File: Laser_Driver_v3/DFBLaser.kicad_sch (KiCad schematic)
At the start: 38 parts, among them Q15 IRLML6344TRPBF, Q16 IRLML6344TRPBF, U23 OPA192IDR, U24 OPA192IDR

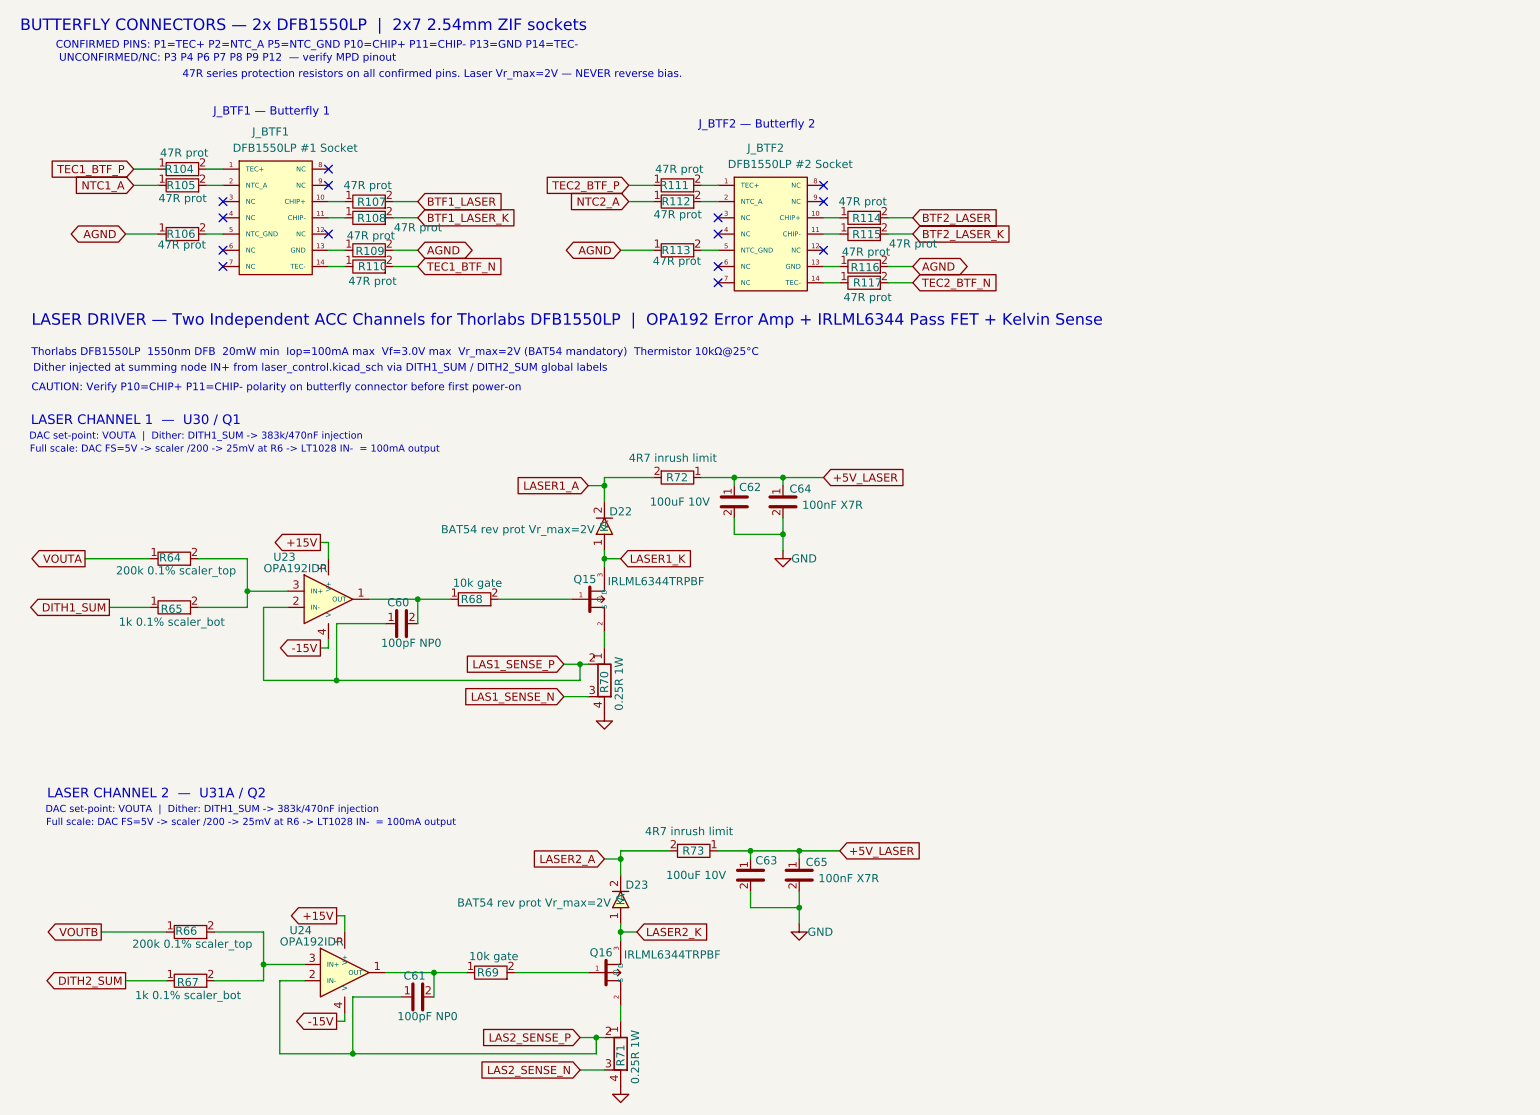
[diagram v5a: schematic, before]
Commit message: Added separate xfrmer for 6V.
Added inrush protection with NTC and increased capacitance to reduce ripple on 6V
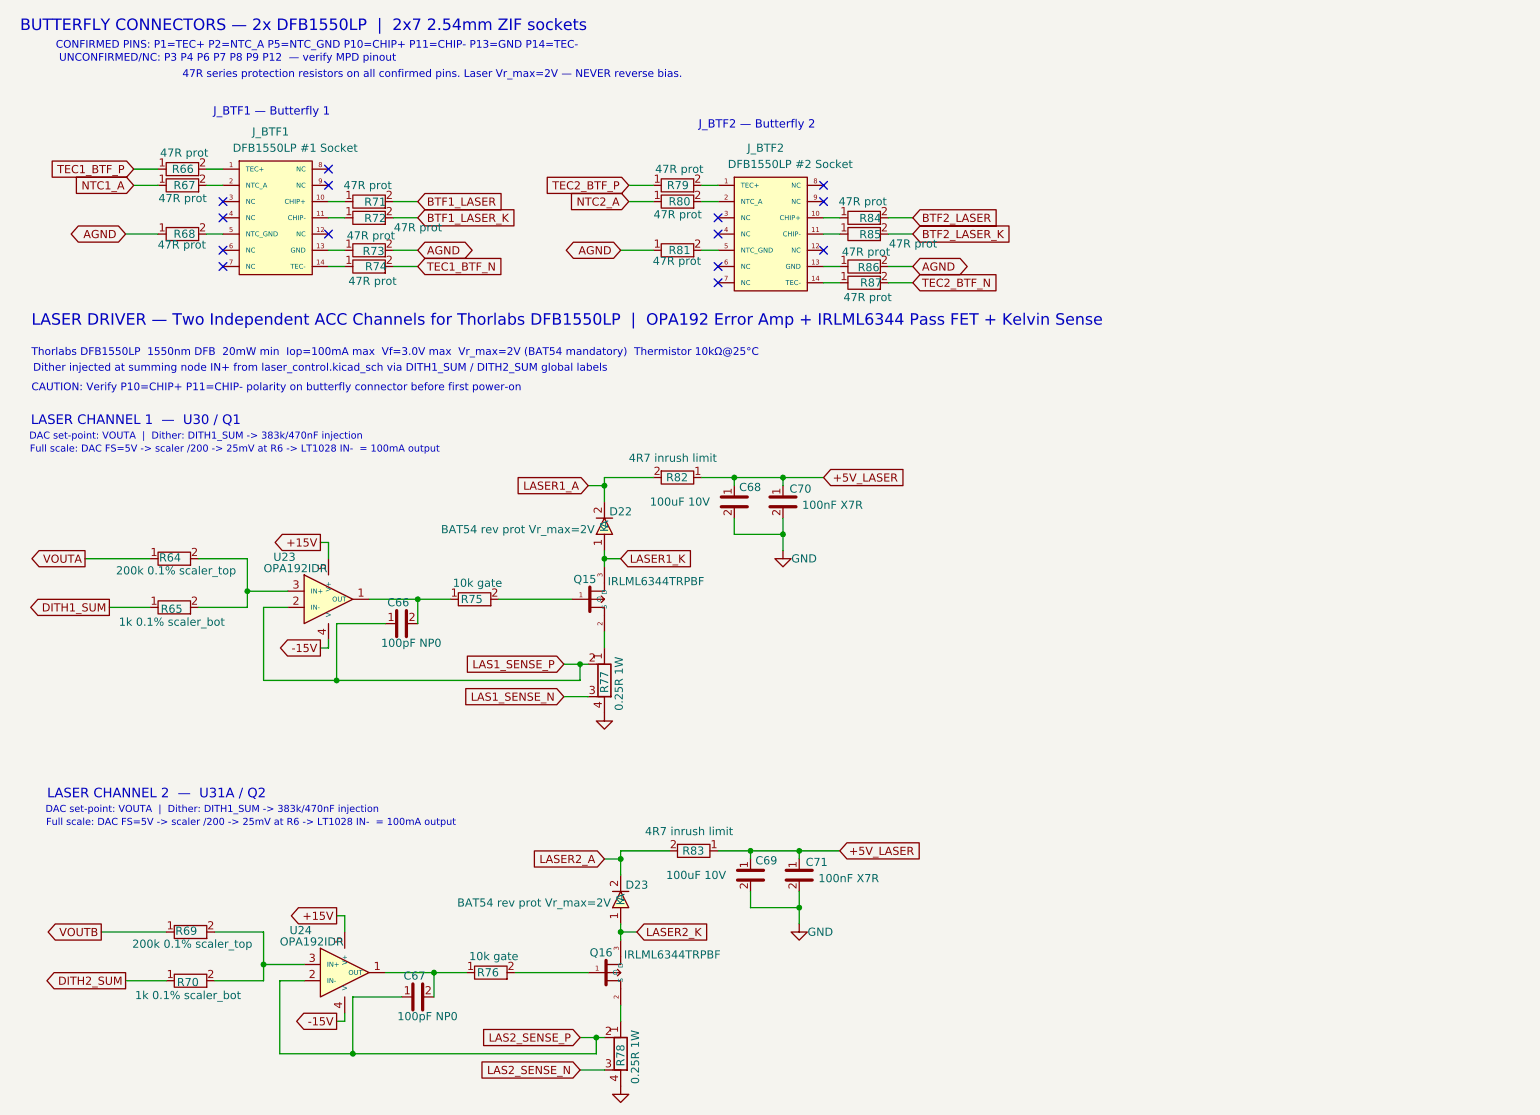
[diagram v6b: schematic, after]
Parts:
- renumbered C60 to C66, C61 to C67, C62 to C68, C63 to C69, C64 to C70, C65 to C71, R104 to R66, R105 to R67, R106 to R68, R66 to R69, R67 to R70, R107 to R71, R108 to R72, R109 to R73, R110 to R74, R68 to R75, R69 to R76, R70 to R77, R71 to R78, R111 to R79, R112 to R80, R113 to R81, R72 to R82, R73 to R83, R114 to R84, R115 to R85, R116 to R86, R117 to R87

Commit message: Changed xfrmers, paralled BJTs for cap multiplier
Changed the transformers to more appropriate voltages.
Made the BJTs for the cap multipliers in parallel to better handle the load.
Simulated the output ripple for the 6V.
Clarifying notes, removed LT1028 changed to OPA192 to match circuit as drawn.
Changed divider values for the TEC_zero value to be 1.2 V as designed.
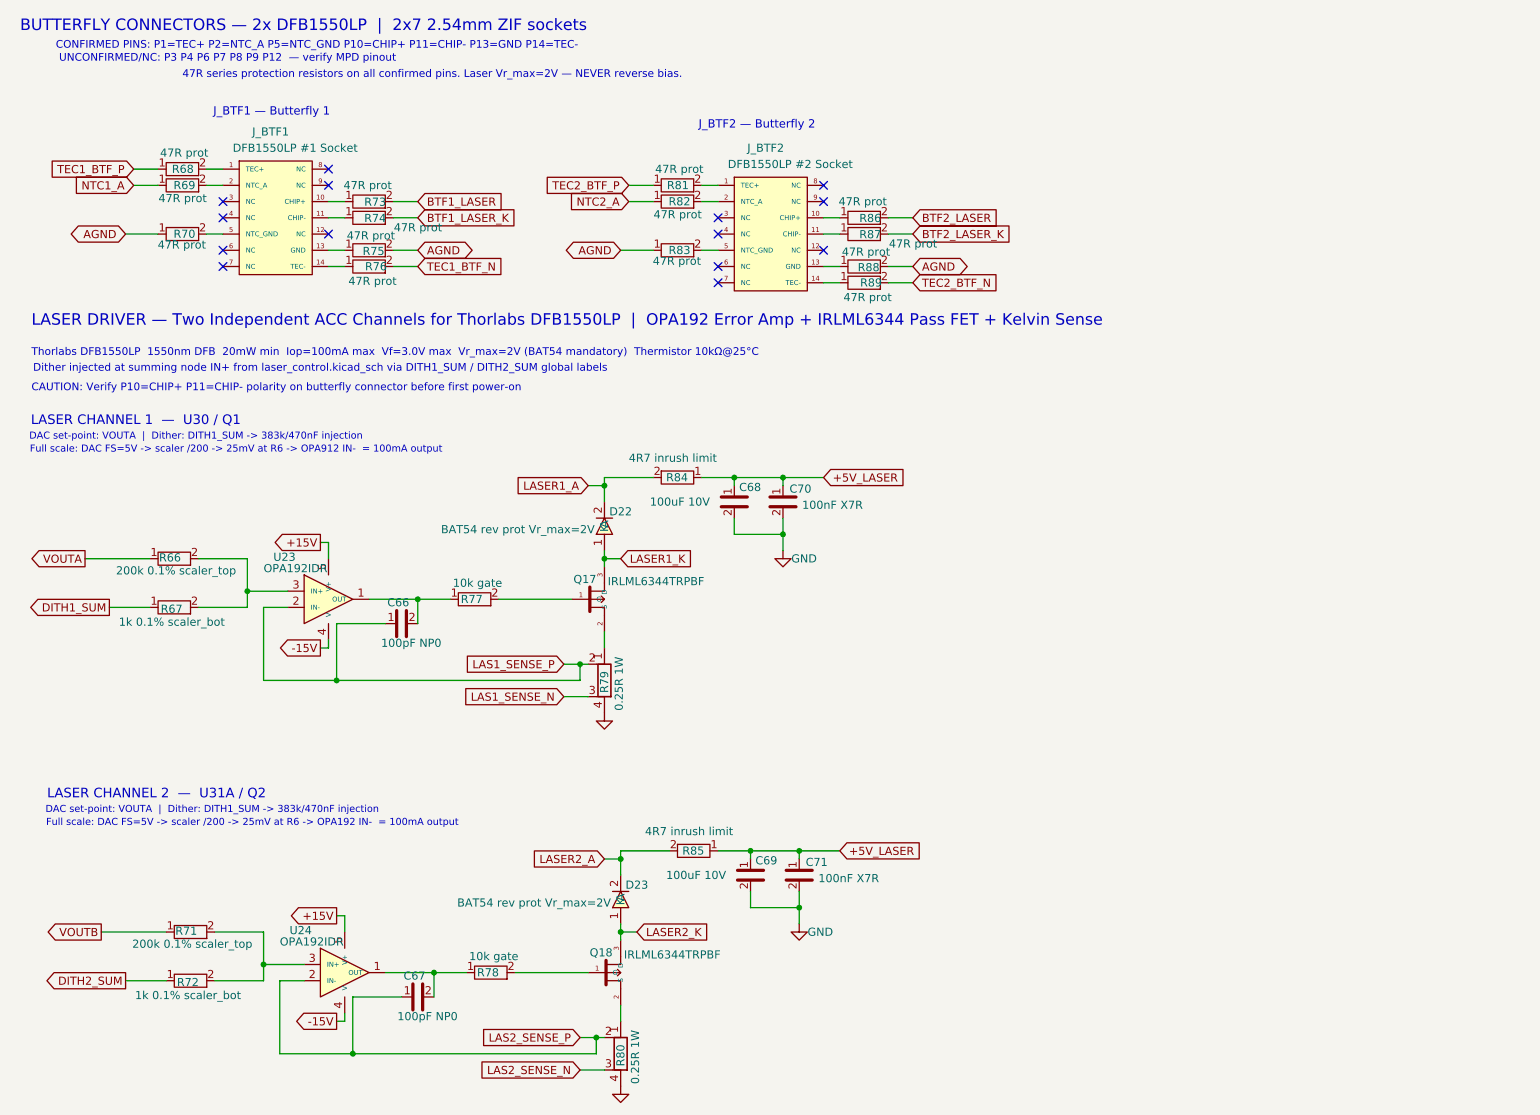
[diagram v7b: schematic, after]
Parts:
- renumbered Q15 to Q17, Q16 to Q18, R64 to R66, R65 to R67, R66 to R68, R67 to R69, R68 to R70, R69 to R71, R70 to R72, R71 to R73, R72 to R74, R73 to R75, R74 to R76, R75 to R77, R76 to R78, R77 to R79, R78 to R80, R79 to R81, R80 to R82, R81 to R83, R82 to R84, R83 to R85, R84 to R86, R85 to R87, R86 to R88, R87 to R89
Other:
- note added: "Full scale: DAC FS=5V -> scaler /200 -> 25mV at R6 -> OPA192 IN- = 100mA output"
- note added: "Full scale: DAC FS=5V -> scaler /200 -> 25mV at R6 -> OPA912 IN- = 100mA output"
- note removed: "Full scale: DAC FS=5V -> scaler /200 -> 25mV at R6 -> LT1028 IN- = 100mA output"
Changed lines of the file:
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@@
 		)
 	)
-	(text "Full scale: DAC FS=5V -> scaler /200 -> 25mV at R6 -> LT1028 IN-  = 100mA output"
+	(text "Full scale: DAC FS=5V -> scaler /200 -> 25mV at R6 -> OPA192 IN-  = 100mA output"
 		(exclude_from_sim no)
 		(at 19.304 140.462 0)
@@
 		)
 	)
-	(text "Full scale: DAC FS=5V -> scaler /200 -> 25mV at R6 -> LT1028 IN-  = 100mA output"
+	(text "Full scale: DAC FS=5V -> scaler /200 -> 25mV at R6 -> OPA912 IN-  = 100mA output"
 		(exclude_from_sim no)
 		(at 16.764 82.042 0)
@@
 		(in_pos_files yes)
 		(dnp no)
-		(property "Reference" "R76"
+		(property "Reference" "R78"
 			(at 90.17 163.83 90)
 			(show_name no)
@@
 			(project "laser_driver_v3"
 				(path "/b2c3d4e5-f6a7-8901-bcde-f12345678901/e4a8b7d8-d294-4c89-ba57-bde3505f7415"
-					(reference "R76")
+					(reference "R78")
 					(unit 1)
 				)
@@
 		(in_pos_files yes)
 		(dnp no)
-		(property "Reference" "R82"
+		(property "Reference" "R84"
 			(at 116.332 86.36 90)
 			(show_name no)
@@
 			(project "laser_driver_v3"
 				(path "/b2c3d4e5-f6a7-8901-bcde-f12345678901/e4a8b7d8-d294-4c89-ba57-bde3505f7415"
-					(reference "R82")
+					(reference "R84")
 					(unit 1)
 				)
@@
 		(in_pos_files yes)
 		(dnp no)
-		(property "Reference" "R67"
+		(property "Reference" "R69"
 			(at 42.672 40.64 90)
 			(show_name no)
@@
 			(project "laser_driver_v3"
 				(path "/b2c3d4e5-f6a7-8901-bcde-f12345678901/e4a8b7d8-d294-4c89-ba57-bde3505f7415"
-					(reference "R67")
+					(reference "R69")
 					(unit 1)
 				)
@@
 		(in_pos_files yes)
 		(dnp no)
-		(property "Reference" "R71"
+		(property "Reference" "R73"
 			(at 72.518 43.246 90)
 			(show_name no)
@@
 			(project "laser_driver_v3"
 				(path "/b2c3d4e5-f6a7-8901-bcde-f12345678901/e4a8b7d8-d294-4c89-ba57-bde3505f7415"
-					(reference "R71")
+					(reference "R73")
 					(unit 1)
 				)
@@
 		(in_pos_files yes)
 		(dnp no)
-		(property "Reference" "Q15"
+		(property "Reference" "Q17"
 			(at 101.826 102.284 0)
 			(show_name no)
@@
 			(project "laser_driver_v3"
 				(path "/b2c3d4e5-f6a7-8901-bcde-f12345678901/e4a8b7d8-d294-4c89-ba57-bde3505f7415"
-					(reference "Q15")
+					(reference "Q17")
 					(unit 1)
 				)
@@
 		(in_pos_files yes)
 		(dnp no)
-		(property "Reference" "Q16"
+		(property "Reference" "Q18"
 			(at 104.366 160.704 0)
 			(show_name no)
@@
 			(project "laser_driver_v3"
 				(path "/b2c3d4e5-f6a7-8901-bcde-f12345678901/e4a8b7d8-d294-4c89-ba57-bde3505f7415"
-					(reference "Q16")
+					(reference "Q18")
 					(unit 1)
 				)
@@
 		(in_pos_files yes)
 		(dnp no)
-		(property "Reference" "R83"
+		(property "Reference" "R85"
 			(at 118.872 144.78 90)
 			(show_name no)
@@
 			(project "laser_driver_v3"
 				(path "/b2c3d4e5-f6a7-8901-bcde-f12345678901/e4a8b7d8-d294-4c89-ba57-bde3505f7415"
-					(reference "R83")
+					(reference "R85")
 					(unit 1)
 				)
@@
 		(in_pos_files yes)
 		(dnp no)
-		(property "Reference" "R81"
+		(property "Reference" "R83"
 			(at 120.142 50.8 90)
 			(show_name no)
@@
 			(project "laser_driver_v3"
 				(path "/b2c3d4e5-f6a7-8901-bcde-f12345678901/e4a8b7d8-d294-4c89-ba57-bde3505f7415"
-					(reference "R81")
+					(reference "R83")
 					(unit 1)
 				)
@@
 		(in_pos_files yes)
 		(dnp no)
-		(property "Reference" "R87"
+		(property "Reference" "R89"
 			(at 150.114 55.88 90)
 			(show_name no)
@@
 			(project "laser_driver_v3"
 				(path "/b2c3d4e5-f6a7-8901-bcde-f12345678901/e4a8b7d8-d294-4c89-ba57-bde3505f7415"
-					(reference "R87")
+					(reference "R89")
 					(unit 1)
 				)
@@
 		(in_pos_files yes)
 		(dnp no)
-		(property "Reference" "R65"
+		(property "Reference" "R67"
 			(at 40.668 106.936 90)
 			(show_name no)
@@
 			(project "laser_driver_v3"
 				(path "/b2c3d4e5-f6a7-8901-bcde-f12345678901/e4a8b7d8-d294-4c89-ba57-bde3505f7415"
-					(reference "R65")
+					(reference "R67")
 					(unit 1)
 				)
@@
 		(in_pos_files yes)
 		(dnp no)
-		(property "Reference" "R66"
+		(property "Reference" "R68"
 			(at 42.418 38.1 90)
 			(show_name no)
@@
 			(project "laser_driver_v3"
 				(path "/b2c3d4e5-f6a7-8901-bcde-f12345678901/e4a8b7d8-d294-4c89-ba57-bde3505f7415"
-					(reference "R66")
+					(reference "R68")
 					(unit 1)
 				)
@@
 		(in_pos_files yes)
 		(dnp no)
-		(property "Reference" "R79"
+		(property "Reference" "R81"
 			(at 119.888 40.64 90)
 			(show_name no)
@@
 			(project "laser_driver_v3"
 				(path "/b2c3d4e5-f6a7-8901-bcde-f12345678901/e4a8b7d8-d294-4c89-ba57-bde3505f7415"
-					(reference "R79")
+					(reference "R81")
 					(unit 1)
 				)
@@
 		(in_pos_files yes)
 		(dnp no)
-		(property "Reference" "R78"
+		(property "Reference" "R80"
 			(at 109.22 176.784 90)
 			(show_name no)
@@
 			(project "laser_driver_v3"
 				(path "/b2c3d4e5-f6a7-8901-bcde-f12345678901/e4a8b7d8-d294-4c89-ba57-bde3505f7415"
-					(reference "R78")
+					(reference "R80")
 					(unit 1)
 				)
@@
 		(in_pos_files yes)
 		(dnp no)
-		(property "Reference" "R69"
+		(property "Reference" "R71"
 			(at 42.954 157.322 90)
 			(show_name no)
@@
 			(project "laser_driver_v3"
 				(path "/b2c3d4e5-f6a7-8901-bcde-f12345678901/e4a8b7d8-d294-4c89-ba57-bde3505f7415"
-					(reference "R69")
+					(reference "R71")
 					(unit 1)
 				)
@@
 		(in_pos_files yes)
 		(dnp no)
-		(property "Reference" "R73"
+		(property "Reference" "R75"
 			(at 72.264 50.946 90)
 			(show_name no)
@@
 			(project "laser_driver_v3"
 				(path "/b2c3d4e5-f6a7-8901-bcde-f12345678901/e4a8b7d8-d294-4c89-ba57-bde3505f7415"
-					(reference "R73")
+					(reference "R75")
 					(unit 1)
 				)
@@
 		(in_pos_files yes)
 		(dnp no)
-		(property "Reference" "R86"
+		(property "Reference" "R88"
 			(at 149.734 53.486 90)
 			(show_name no)
@@
 			(project "laser_driver_v3"
 				(path "/b2c3d4e5-f6a7-8901-bcde-f12345678901/e4a8b7d8-d294-4c89-ba57-bde3505f7415"
-					(reference "R86")
+					(reference "R88")
 					(unit 1)
 				)
@@
 		(in_pos_files yes)
 		(dnp no)
-		(property "Reference" "R80"
+		(property "Reference" "R82"
 			(at 120.142 43.18 90)
 			(show_name no)
@@
 			(project "laser_driver_v3"
 				(path "/b2c3d4e5-f6a7-8901-bcde-f12345678901/e4a8b7d8-d294-4c89-ba57-bde3505f7415"
-					(reference "R80")
+					(reference "R82")
 					(unit 1)
 				)
@@
 		(in_pos_files yes)
 		(dnp no)
-		(property "Reference" "R74"
+		(property "Reference" "R76"
 			(at 72.644 53.34 90)
 			(show_name no)
@@
 			(project "laser_driver_v3"
 				(path "/b2c3d4e5-f6a7-8901-bcde-f12345678901/e4a8b7d8-d294-4c89-ba57-bde3505f7415"
-					(reference "R74")
+					(reference "R76")
 					(unit 1)
 				)
@@
 		(in_pos_files yes)
 		(dnp no)
-		(property "Reference" "R77"
+		(property "Reference" "R79"
 			(at 106.68 118.364 90)
 			(show_name no)
@@
 			(project "laser_driver_v3"
 				(path "/b2c3d4e5-f6a7-8901-bcde-f12345678901/e4a8b7d8-d294-4c89-ba57-bde3505f7415"
-					(reference "R77")
+					(reference "R79")
 					(unit 1)
 				)
@@
 		(in_pos_files yes)
 		(dnp no)
-		(property "Reference" "R68"
+		(property "Reference" "R70"
 			(at 42.672 48.26 90)
 			(show_name no)
@@
 			(project "laser_driver_v3"
 				(path "/b2c3d4e5-f6a7-8901-bcde-f12345678901/e4a8b7d8-d294-4c89-ba57-bde3505f7415"
-					(reference "R68")
+					(reference "R70")
 					(unit 1)
 				)
@@
 		(in_pos_files yes)
 		(dnp no)
-		(property "Reference" "R72"
+		(property "Reference" "R74"
 			(at 72.518 45.786 90)
 			(show_name no)
@@
 			(project "laser_driver_v3"
 				(path "/b2c3d4e5-f6a7-8901-bcde-f12345678901/e4a8b7d8-d294-4c89-ba57-bde3505f7415"
-					(reference "R72")
+					(reference "R74")
 					(unit 1)
 				)
@@
 		(in_pos_files yes)
 		(dnp no)
-		(property "Reference" "R64"
+		(property "Reference" "R66"
 			(at 40.414 98.902 90)
 			(show_name no)
@@
 			(project "laser_driver_v3"
 				(path "/b2c3d4e5-f6a7-8901-bcde-f12345678901/e4a8b7d8-d294-4c89-ba57-bde3505f7415"
-					(reference "R64")
+					(reference "R66")
 					(unit 1)
 				)
@@
 		(in_pos_files yes)
 		(dnp no)
-		(property "Reference" "R85"
+		(property "Reference" "R87"
 			(at 149.988 48.326 90)
 			(show_name no)
@@
 			(project "laser_driver_v3"
 				(path "/b2c3d4e5-f6a7-8901-bcde-f12345678901/e4a8b7d8-d294-4c89-ba57-bde3505f7415"
-					(reference "R85")
+					(reference "R87")
 					(unit 1)
 				)
@@
 		(in_pos_files yes)
 		(dnp no)
-		(property "Reference" "R70"
+		(property "Reference" "R72"
 			(at 43.208 165.356 90)
 			(show_name no)
@@
 			(project "laser_driver_v3"
 				(path "/b2c3d4e5-f6a7-8901-bcde-f12345678901/e4a8b7d8-d294-4c89-ba57-bde3505f7415"
-					(reference "R70")
+					(reference "R72")
 					(unit 1)
 				)
@@
 		(in_pos_files yes)
 		(dnp no)
-		(property "Reference" "R84"
+		(property "Reference" "R86"
 			(at 149.988 45.786 90)
 			(show_name no)
@@
 			(project "laser_driver_v3"
 				(path "/b2c3d4e5-f6a7-8901-bcde-f12345678901/e4a8b7d8-d294-4c89-ba57-bde3505f7415"
-					(reference "R84")
+					(reference "R86")
 					(unit 1)
 				)
@@
 		(in_pos_files yes)
 		(dnp no)
-		(property "Reference" "R75"
+		(property "Reference" "R77"
 			(at 87.63 105.41 90)
 			(show_name no)
@@
 			(project "laser_driver_v3"
 				(path "/b2c3d4e5-f6a7-8901-bcde-f12345678901/e4a8b7d8-d294-4c89-ba57-bde3505f7415"
-					(reference "R75")
+					(reference "R77")
 					(unit 1)
 				)
